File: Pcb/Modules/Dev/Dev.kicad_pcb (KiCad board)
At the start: 2 copper layers, 50.8 x 20.3 mm, 12 parts, among them J1 JACK_STEREO, J2 JACK_RJ45, P1 CONN_02X04, Q1 Q_NMOS_GSD, SW0 SW_TACTILE, X1 HOLE, X2 HOLE, X3 HOLE, X4 HOLE

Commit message: Update pcbs.
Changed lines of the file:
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@@
   (gr_line (start 25.4 31.75) (end 25.4 39.37) (angle 90) (layer Edge.Cuts) (width 0.15))
   (gr_line (start 76.2 31.75) (end 76.2 39.37) (angle 90) (layer Edge.Cuts) (width 0.15))
-  (gr_text "Dev Module\n2017-10-11" (at 60.706 27.94) (layer F.SilkS)
+  (gr_text "Dev Module\n2017-10-11" (at 63.246 27.94) (layer F.SilkS)
     (effects (font (size 1.27 1.27) (thickness 0.254)) (justify left))
   )

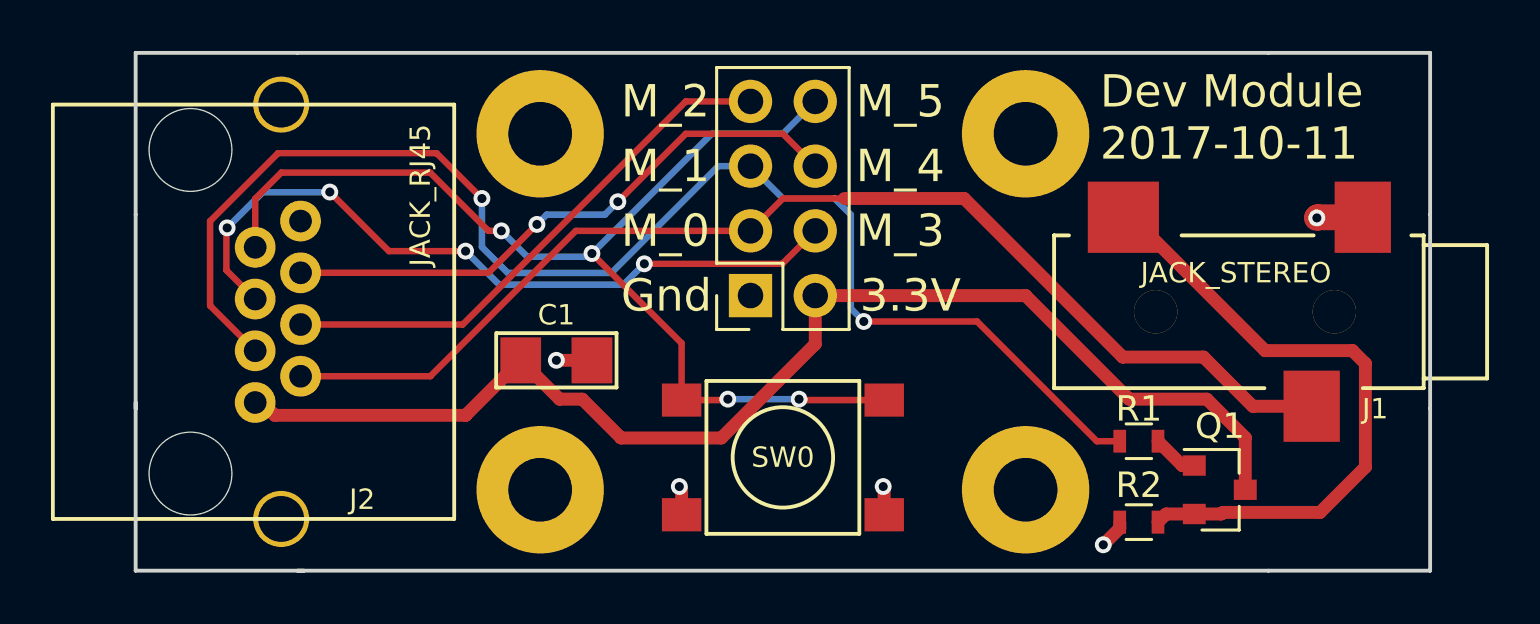
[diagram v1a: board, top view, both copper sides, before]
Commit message: Update PCBs to use n channel mosfet on low side
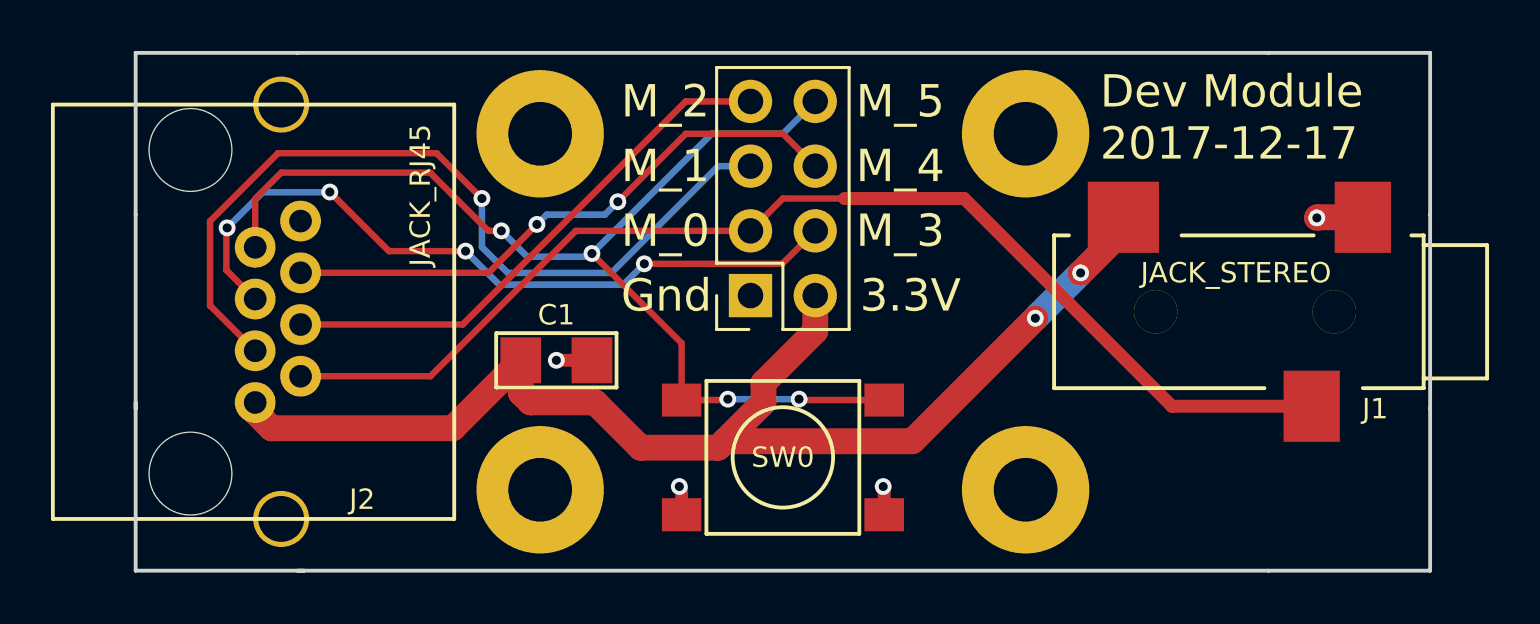
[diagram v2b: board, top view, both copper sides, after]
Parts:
- removed Q1: Q_NMOS_GSD, TO_SOT_Packages_SMD:SOT-23
- removed R1: 1K, Resistors_SMD:R_0603
- removed R2: 10K, Resistors_SMD:R_0603
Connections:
- J1 pad 2: Net-(J1-Pad2) -> 3V3
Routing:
- net Net-(J1-Pad2): track 25.0 -> 0.00 mm
- net /M_1: track 54.1 -> 32.9 mm, vias 2 -> 1
- net Net-(Q1-Pad1): track 1.82 -> 0.00 mm
- net GND: track 6.63 -> 5.48 mm, vias 5 -> 4
- net 3V3: track 49.0 -> 49.8 mm, vias 0 -> 2
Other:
- board text added: "Dev Module 2017-12-17"
- board text removed: "Dev Module 2017-10-11"

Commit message: Update CA6 PCB.  Also update versions of all the module pcbs to match.
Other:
- board text added: "Dev Module 2017.12.23"
- board text removed: "Dev Module 2017-12-17"
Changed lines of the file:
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@@
     (links 19)
     (no_connects 0)
-    (area 25.324999 25.324999 76.275001 45.795001)
+    (area 21.873869 23.9968 78.714601 47.1232)
     (thickness 1.6)
     (drawings 21)
@@
   )
   (setup
-    (last_trace_width 0.508)
+    (last_trace_width 0.254)
     (user_trace_width 0.508)
     (user_trace_width 1.016)
@@
   (gr_line (start 25.4 31.75) (end 25.4 39.37) (angle 90) (layer Edge.Cuts) (width 0.15))
   (gr_line (start 76.2 31.75) (end 76.2 39.37) (angle 90) (layer Edge.Cuts) (width 0.15))
-  (gr_text "Dev Module\n2017-12-17" (at 63.246 27.94) (layer F.SilkS)
+  (gr_text "Dev Module\n2017.12.23" (at 63.246 27.94) (layer F.SilkS)
     (effects (font (size 1.27 1.27) (thickness 0.254)) (justify left))
   )

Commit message: Move holes on sound module to match other modules.  Updated silkscreens on other modules.  Generate gerbers
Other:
- board text added: "Dev Module 2018.3.31"
- board text removed: "Dev Module 2017.12.23"
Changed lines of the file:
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@@
   (gr_line (start 25.4 31.75) (end 25.4 39.37) (angle 90) (layer Edge.Cuts) (width 0.15))
   (gr_line (start 76.2 31.75) (end 76.2 39.37) (angle 90) (layer Edge.Cuts) (width 0.15))
-  (gr_text "Dev Module\n2017.12.23" (at 63.246 27.94) (layer F.SilkS)
+  (gr_text "Dev Module\n2018.3.31" (at 63.246 27.94) (layer F.SilkS)
     (effects (font (size 1.27 1.27) (thickness 0.254)) (justify left))
   )

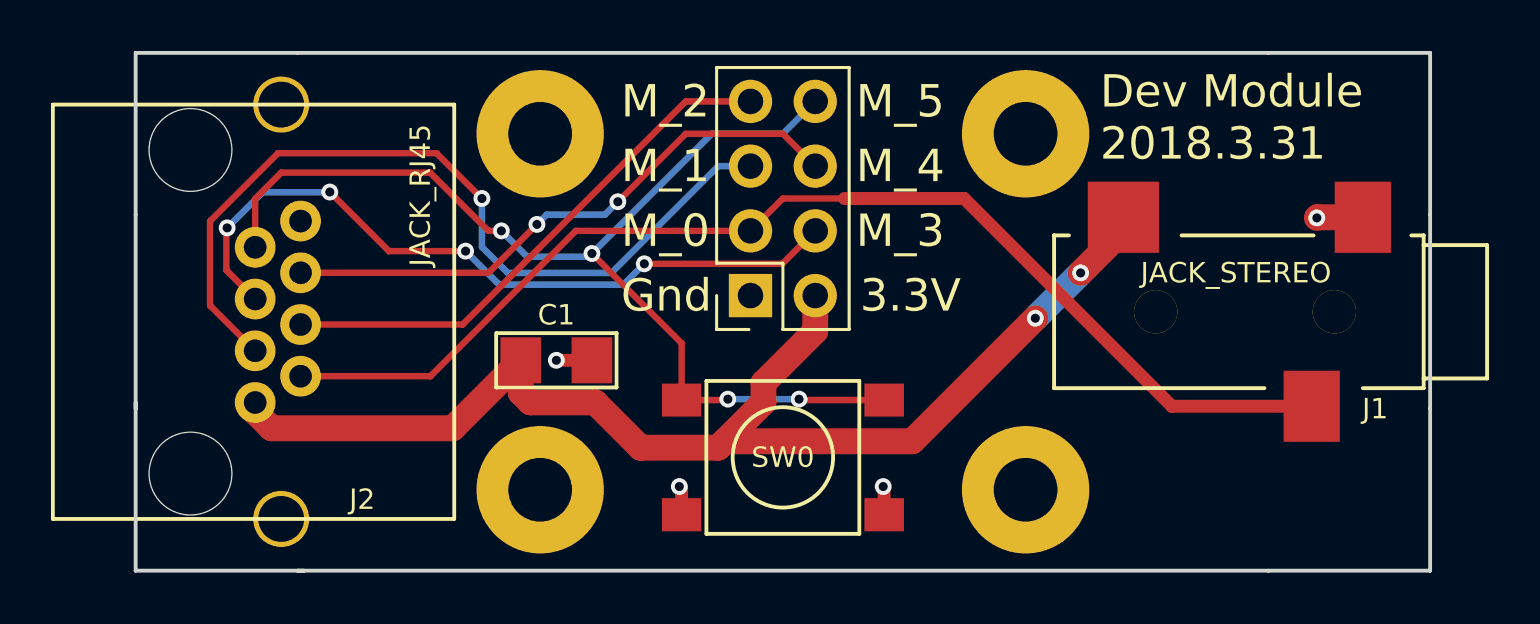
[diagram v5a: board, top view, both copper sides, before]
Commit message: Update module pcbs to fix minor issues and round corners
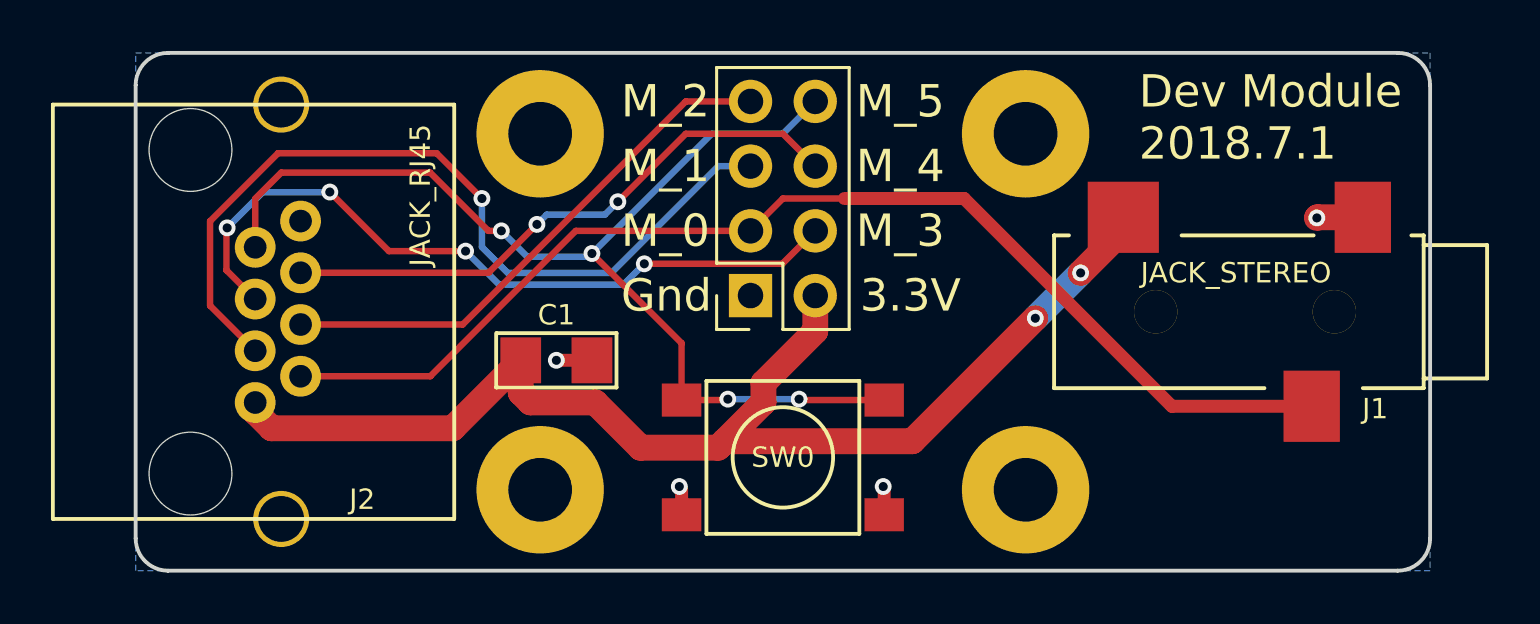
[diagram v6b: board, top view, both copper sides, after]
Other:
- outline, holes or cut-outs redrawn
- board text added: "Dev Module 2018.7.1"
- board text removed: "Dev Module 2018.3.31"
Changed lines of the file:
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@@
     (area 21.873869 23.9968 78.714601 47.1232)
     (thickness 1.6)
-    (drawings 21)
+    (drawings 17)
     (tracks 106)
     (zones 0)
@@
     (pad 1 thru_hole circle (at 0 0) (size 5 5) (drill 2.5) (layers *.Cu *.Mask))
   )
-  (gr_line (start 76.2 25.4) (end 76.2 31.75) (angle 90) (layer Edge.Cuts) (width 0.15))
-  (gr_line (start 69.85 25.4) (end 76.2 25.4) (angle 90) (layer Edge.Cuts) (width 0.15))
-  (gr_line (start 76.2 45.72) (end 69.85 45.72) (angle 90) (layer Edge.Cuts) (width 0.15))
-  (gr_line (start 76.2 39.37) (end 76.2 45.72) (angle 90) (layer Edge.Cuts) (width 0.15))
-  (gr_line (start 25.4 25.4) (end 25.4 31.75) (angle 90) (layer Edge.Cuts) (width 0.15))
-  (gr_line (start 31.75 25.4) (end 25.4 25.4) (angle 90) (layer Edge.Cuts) (width 0.15))
-  (gr_line (start 25.4 45.72) (end 25.4 39.116) (angle 90) (layer Edge.Cuts) (width 0.15))
-  (gr_line (start 32.004 45.72) (end 25.4 45.72) (angle 90) (layer Edge.Cuts) (width 0.15))
-  (gr_line (start 25.4 31.75) (end 25.4 39.37) (angle 90) (layer Edge.Cuts) (width 0.15))
-  (gr_line (start 76.2 31.75) (end 76.2 39.37) (angle 90) (layer Edge.Cuts) (width 0.15))
-  (gr_text "Dev Module\n2018.3.31" (at 63.246 27.94) (layer F.SilkS)
+  (gr_line (start 25.4 44.45) (end 25.4 26.67) (angle 90) (layer Edge.Cuts) (width 0.15))
+  (gr_line (start 74.93 45.72) (end 26.67 45.72) (angle 90) (layer Edge.Cuts) (width 0.15))
+  (gr_line (start 76.2 26.67) (end 76.2 44.45) (angle 90) (layer Edge.Cuts) (width 0.15))
+  (gr_line (start 26.67 25.4) (end 74.93 25.4) (angle 90) (layer Edge.Cuts) (width 0.15))
+  (gr_arc (start 26.67 44.45) (end 26.67 45.72) (angle 90) (layer Edge.Cuts) (width 0.15))
+  (gr_arc (start 74.93 44.45) (end 76.2 44.45) (angle 90) (layer Edge.Cuts) (width 0.15))
+  (gr_arc (start 74.93 26.67) (end 74.93 25.4) (angle 90) (layer Edge.Cuts) (width 0.15))
+  (gr_arc (start 26.67 26.67) (end 25.4 26.67) (angle 90) (layer Edge.Cuts) (width 0.15))
+  (gr_text "Dev Module\n2018.7.1" (at 64.77 27.94) (layer F.SilkS)
     (effects (font (size 1.27 1.27) (thickness 0.254)) (justify left))
   )
@@
     (effects (font (size 1.27 1.27) (thickness 0.254)) (justify left))
   )
-  (gr_line (start 69.85 45.72) (end 31.75 45.72) (angle 90) (layer Edge.Cuts) (width 0.15))
-  (gr_line (start 31.75 25.4) (end 69.85 25.4) (angle 90) (layer Edge.Cuts) (width 0.15))
   (segment (start 48.514 40.64) (end 55.88 40.64) (width 1.016) (layer F.Cu) (net 1))
   (segment (start 62.484 34.036) (end 64.1604 32.3596) (width 1.016) (layer F.Cu) (net 1) (status 20))
